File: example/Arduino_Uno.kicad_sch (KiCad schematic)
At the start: 4 parts, among them J1 Power, J2 Digital/PWM, J3 Analog, J4 Digital/PWM

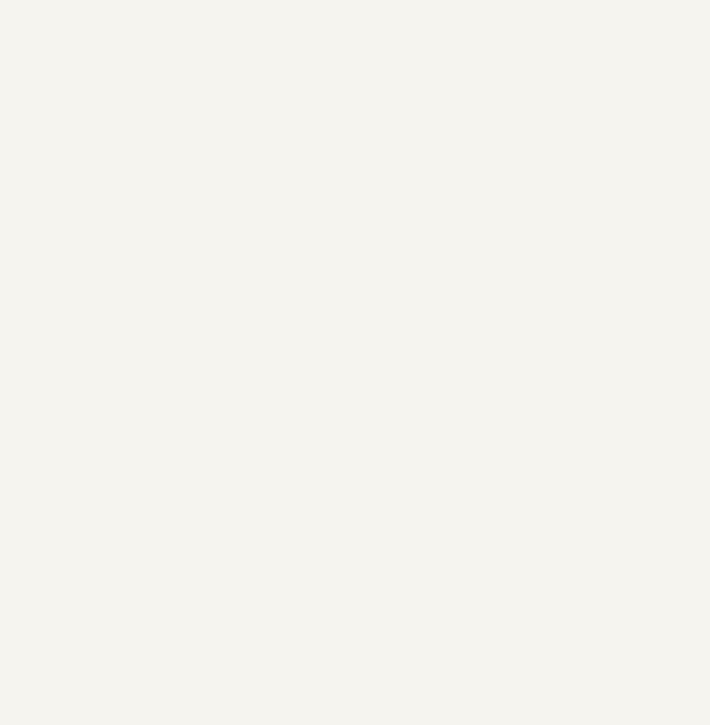
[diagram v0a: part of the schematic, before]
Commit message: Add SSD1306 OLED display to example (test diff feature)
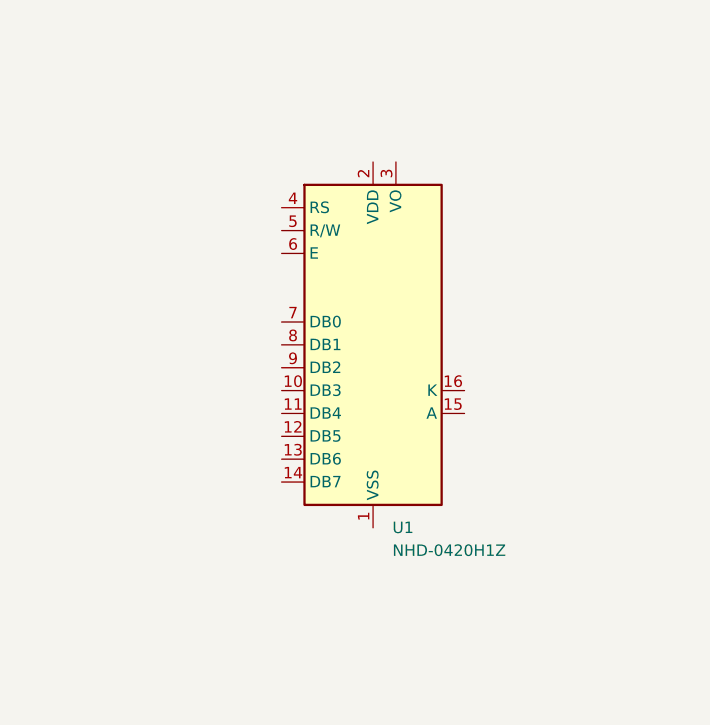
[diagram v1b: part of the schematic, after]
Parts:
- added U1: NHD-0420H1Z, Display:Adafruit_SSD1306, symbol Display_Character:NHD-0420H1Z
